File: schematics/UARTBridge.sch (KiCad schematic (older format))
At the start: 8 parts, among them U15 CP2102N, U16 SP0503BAHT

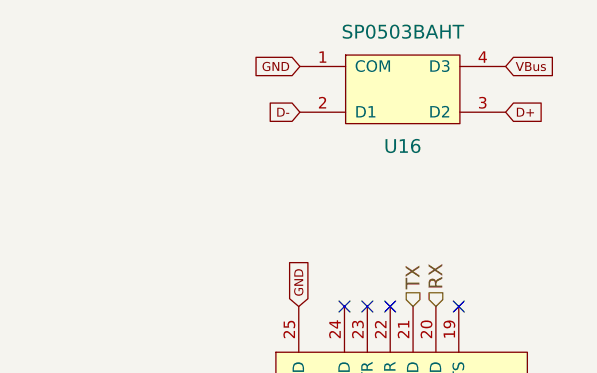
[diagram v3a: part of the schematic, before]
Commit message: refactor: moved circuit protection to main sch
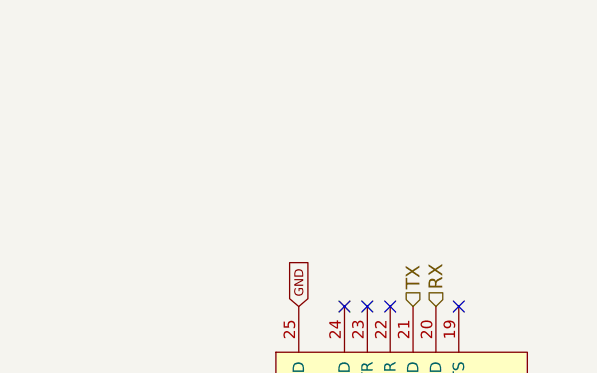
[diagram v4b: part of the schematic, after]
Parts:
- removed U16: SP0503BAHT, Package_TO_SOT_SMD:SOT-143, symbol PSLab:SP0503BAHT
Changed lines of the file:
@@
 $Descr A4 11693 8268
 encoding utf-8
-Sheet 4 3
+Sheet 3 3
 Title "CPN2102N UART Bridge"
 Date "2019-03-03"
@@
 NoConn ~ 6070 4785
 NoConn ~ 5970 4785
-$Comp
-L PSLab:SP0503BAHT U16
-U 1 1 5C4FEC85
-P 5925 2335
-F 0 "U16" H 5925 2085 60  0000 C CNN
-F 1 "SP0503BAHT" H 5925 2585 60  0000 C CNN
-F 2 "Package_TO_SOT_SMD:SOT-143" H 5925 2335 60  0001 C CNN
-F 3 "https://eu.mouser.com/datasheet/2/240/Littelfuse_TVS_Diode_Array_SP05_Datasheet.pdf-777043.pdf" H 5925 2335 60  0001 C CNN
-F 4 "SOT-143" H 5925 2335 50  0001 C CNN "Description"
-F 5 "SP0503BAHTG" H 5925 2335 50  0001 C CNN "Mfr No."
-F 6 "SP0503BAHTG" H 5925 2335 50  0001 C CNN "PartNumber"
-F 7 "0.8" H 5925 2335 50  0001 C CNN "Price"
-	1    5925 2335
-	1    0    0    -1
-$EndComp
 Text HLabel 2370 2630 0    60   Input ~ 0
 GND
@@
 Wire Wire Line
 	2435 2630 2370 2630
-Text GLabel 5475 2235 0    39   Input ~ 0
-GND
 Text GLabel 5470 3285 1    39   Input ~ 0
 GND
@@
 Text HLabel 6070 3285 1    60   Input ~ 0
 RX
-Text GLabel 6375 2435 2    39   Input ~ 0
-D+
-Text GLabel 5475 2435 0    39   Input ~ 0
-D-
-Text GLabel 6375 2235 2    39   Input ~ 0
-VBus
 Text GLabel 4095 4285 0    39   Input ~ 0
 3.3V
